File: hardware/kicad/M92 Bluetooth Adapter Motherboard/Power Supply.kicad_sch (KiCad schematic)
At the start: 32 parts, among them IC2 L7805CDT-TR, IC4 NJU7031D, IC4 TL7660IDR, J1 Conn_External_Power, J4 B2B-XH-A, J5 B2B-XH-A, J9 B6B-XH-A, K3 HE3621A1210, K4 HE3621A1210, Q2 PN2222ATA

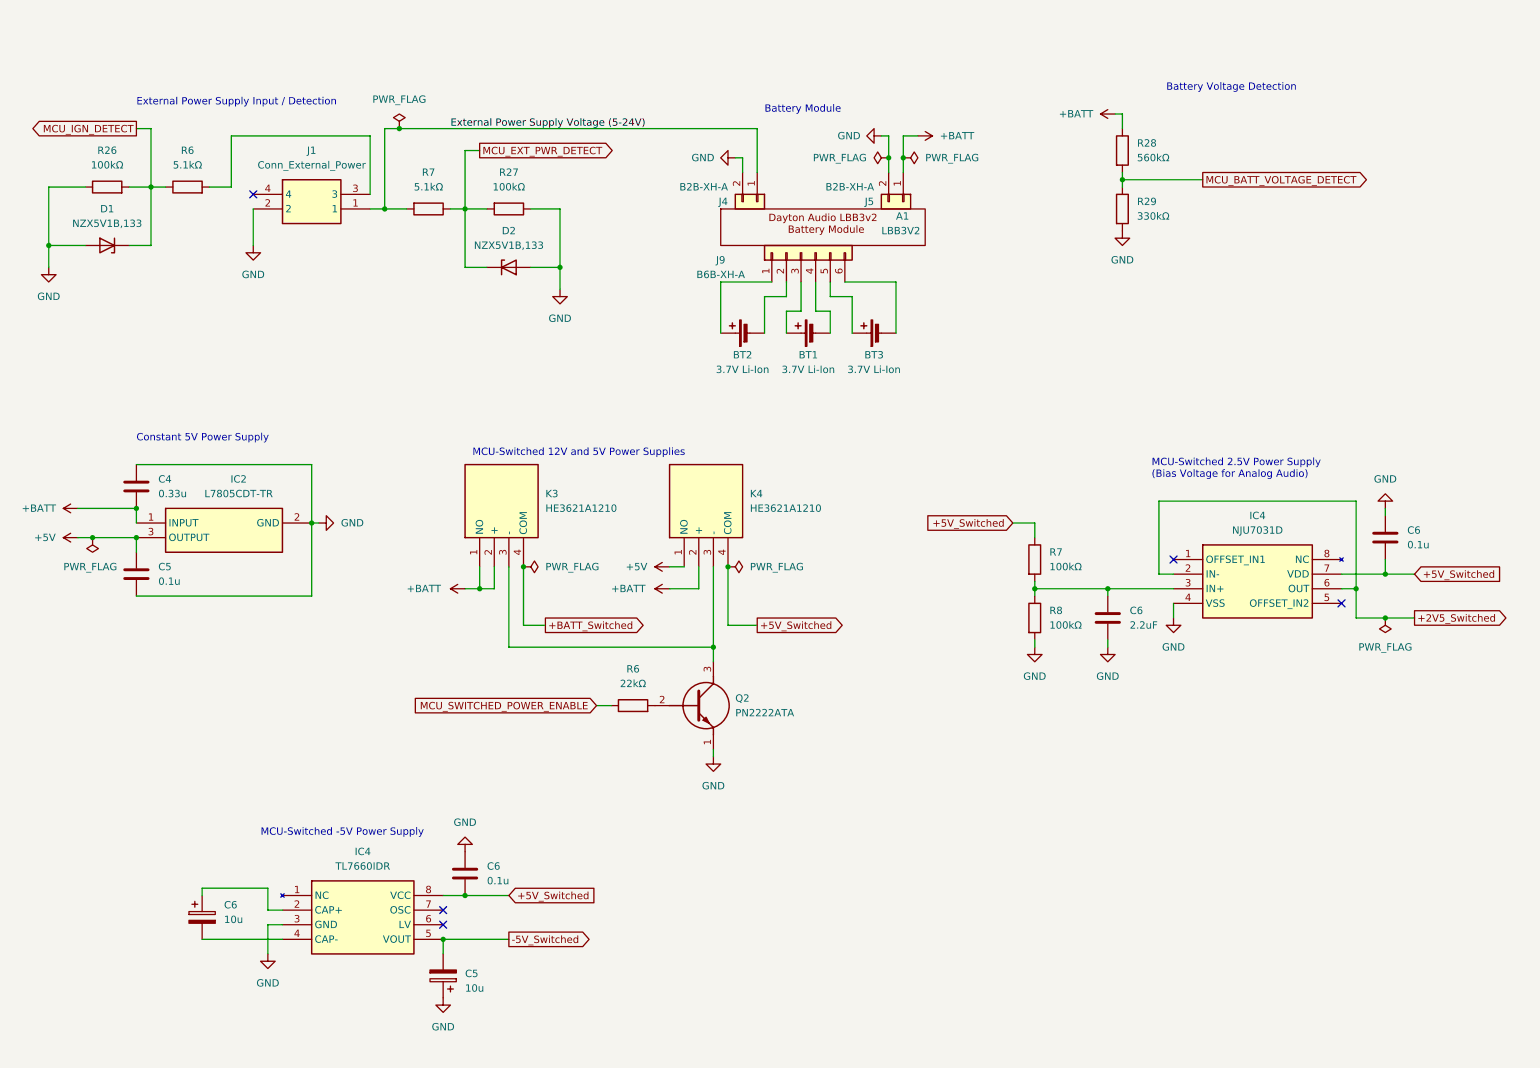
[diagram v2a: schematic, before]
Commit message: Update circuit/PCB to use different power supply/switching components
* Use more efficient 5V regulator.
* Use load switch ICs instead of reed switch relays for power switching.
* Swapped MCU pins for battery voltage detect and power switching for better PCB layout.
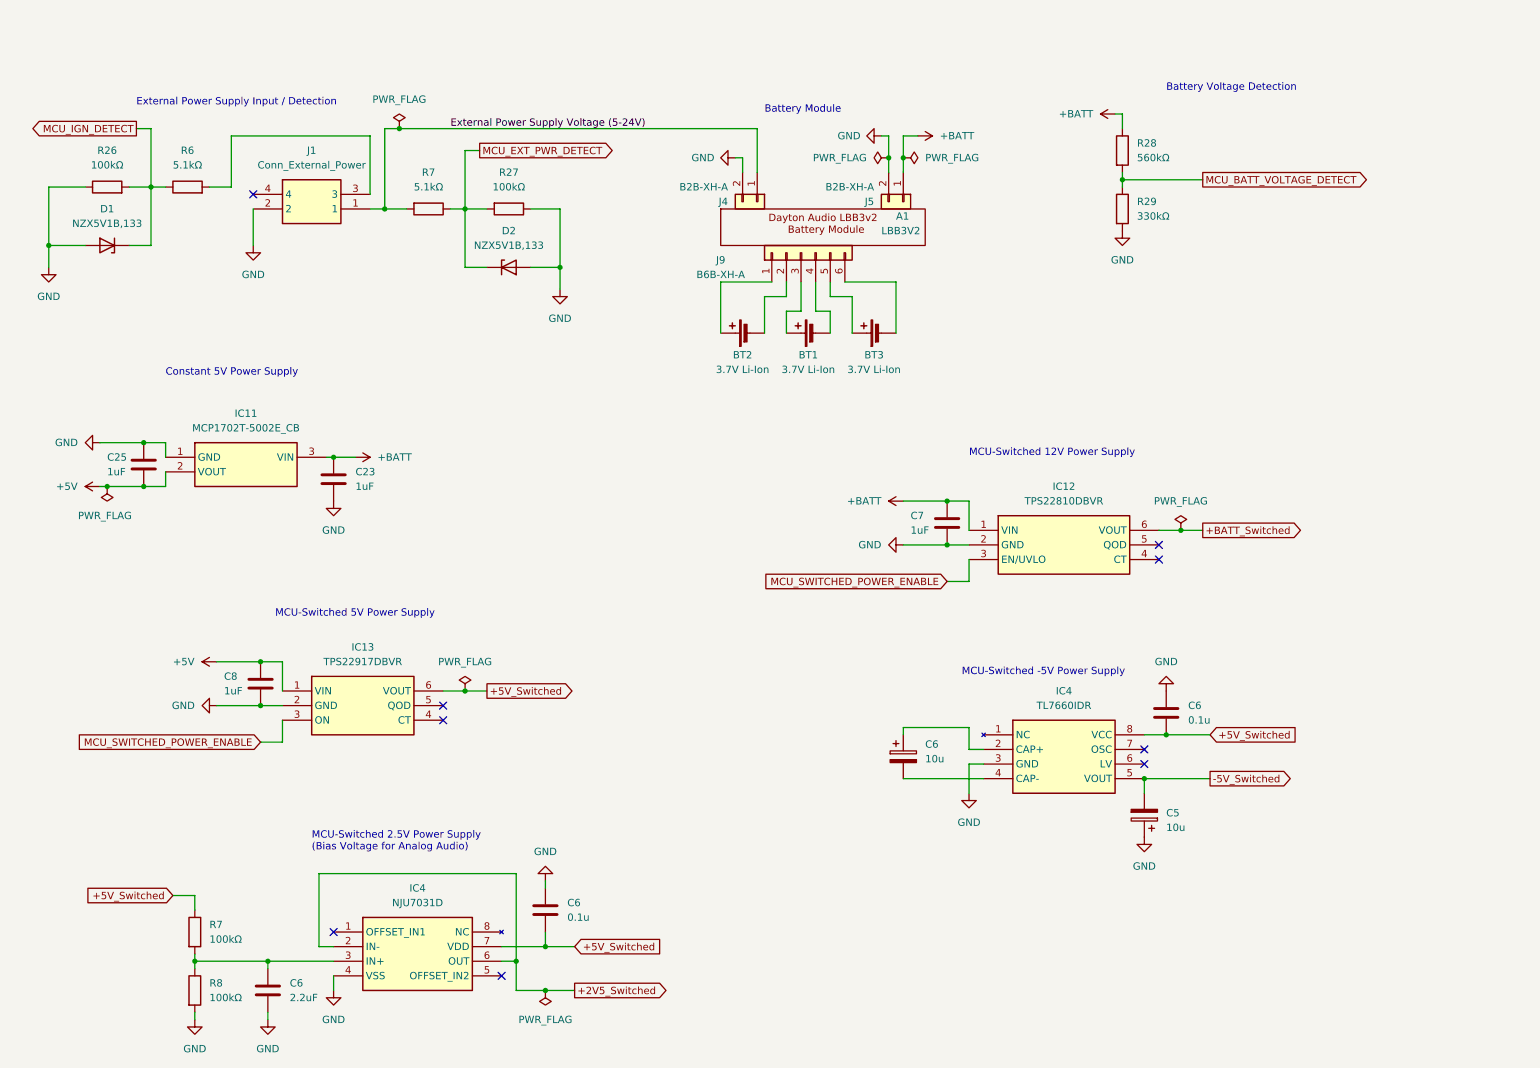
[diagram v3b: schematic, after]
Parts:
- removed C4: 0.33u, Capacitor_SMD:C_1206_3216Metric_Pad1.33x1.80mm_HandSolder, symbol Device:C
- removed C5: 0.1u, Capacitor_SMD:C_1206_3216Metric_Pad1.33x1.80mm_HandSolder, symbol Device:C
- removed IC2: L7805CDT-TR, L7805CDTTR, symbol SamacSys_Parts:L7805CDT-TR
- removed K3, K4: HE3621A1210, HE3621A1210, symbol SamacSys_Parts:HE3621A1210
- removed Q2: PN2222ATA, BC33740TA, symbol SamacSys_Parts:PN2222ATA
- removed R6: 22kΩ, Resistor_SMD:R_1206_3216Metric_Pad1.30x1.75mm_HandSolder, symbol Device:R
- added C23, C25, C7, C8: 1uF, Capacitor_SMD:C_1206_3216Metric_Pad1.33x1.80mm_HandSolder, symbol Device:C
- added IC11: MCP1702T-5002E_CB, SOT95P255X145-3N, symbol SamacSys_Parts:MCP1702T-5002E_CB
- added IC12: TPS22810DBVR, SOT95P280X145-6N, symbol SamacSys_Parts:TPS22810DBVR
- added IC13: TPS22917DBVR, SOT95P280X145-6N, symbol SamacSys_Parts:TPS22917DBVR
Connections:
- net +5V: now also C25.2, C8.1, IC11.2 (VOUT), IC13.1 (VIN)
- net +5V_Switched: now also IC13.6 (VOUT)
- net +BATT: now also C23.1, C7.1, IC11.3 (VIN), IC12.1 (VIN)
- net +BATT_Switched: now also IC12.6 (VOUT)
- net GND: now also C23.2, C25.1, C7.2, C8.2, IC11.1 (GND), IC12.2 (GND), IC13.2 (GND)
- net MCU_SWITCHED_POWER_ENABLE: now also IC12.3 (EN/UVLO), IC13.3 (ON)
- no-connect marks 5 -> 9
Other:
- note added: "MCU-Switched 12V Power Supply"
- note added: "MCU-Switched 5V Power Supply"
- note removed: "MCU-Switched 12V and 5V Power Supplies"
- moved on the sheet: C5, C6, IC4, R7, R8

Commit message: Motherboard circuit/PCB adjustments
* Add 100uf cap to stabilize the 5V power supply (reduce voltage dip during power-on of switched 5V supply).
* Add cap to 12V load switch to reduce inrush current when powering on handset.
* Part number updates to more readily available parts.
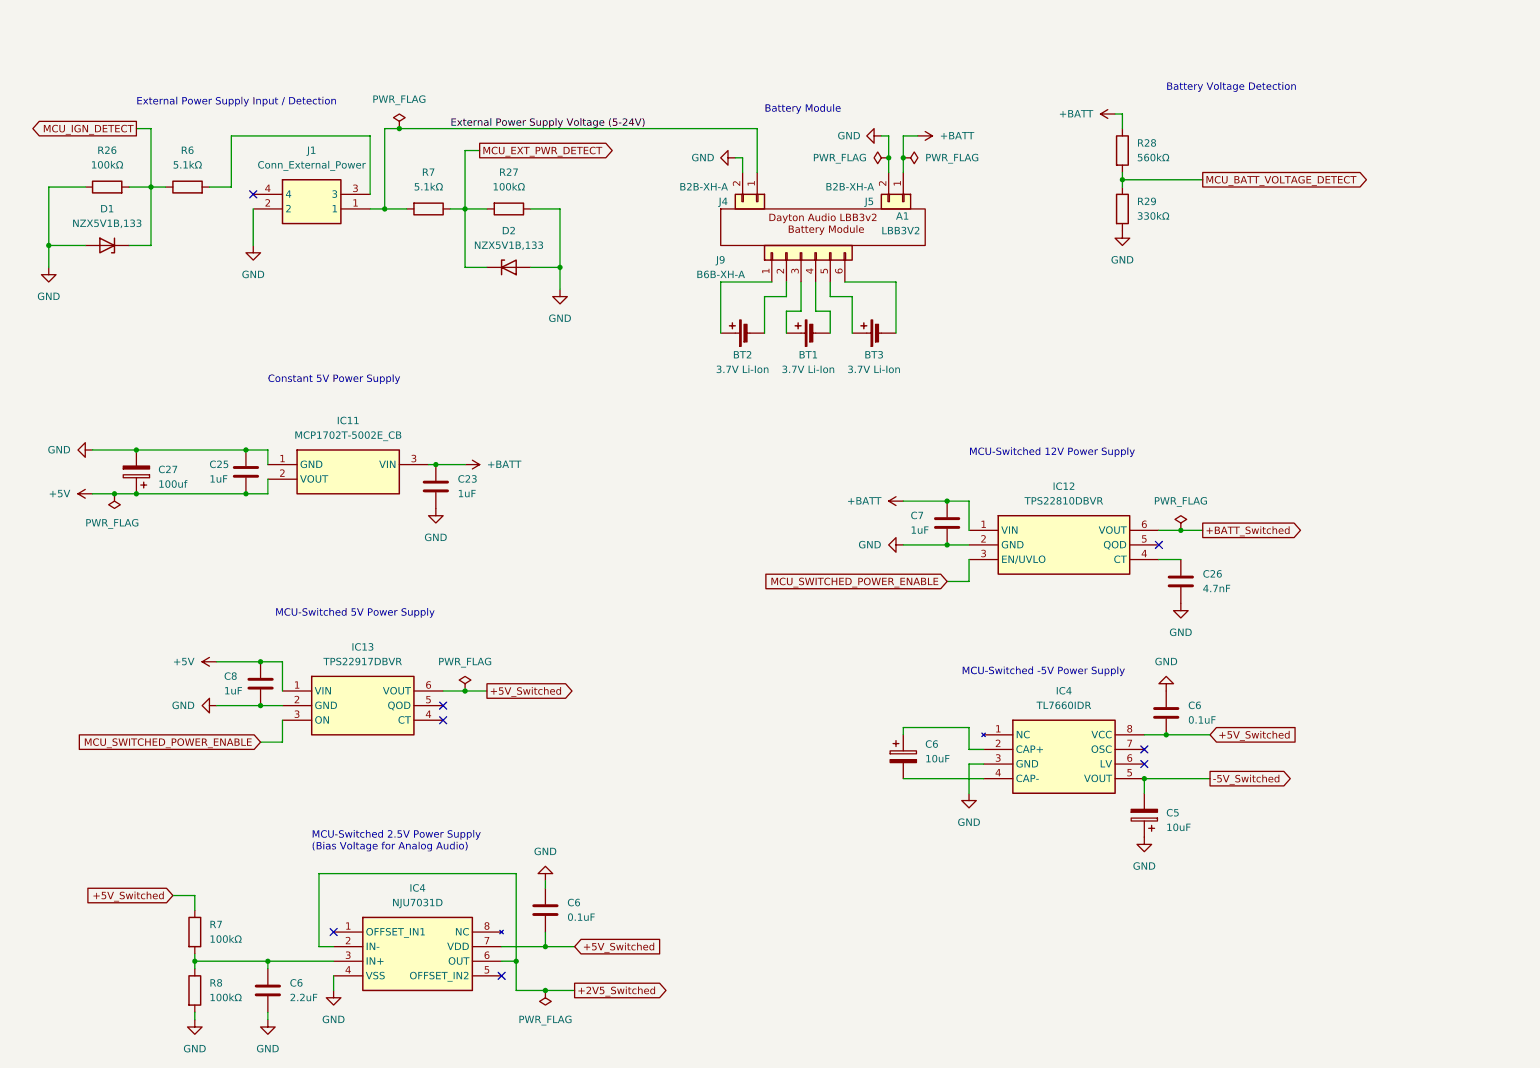
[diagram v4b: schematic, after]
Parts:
- added C26: 4.7nF, Capacitor_SMD:C_1206_3216Metric_Pad1.33x1.80mm_HandSolder, symbol Device:C
- added C27: 100uf, Capacitor_SMD:CP_Elec_5x5.4, symbol Device:C_Polarized
- C5, C6: value 10u -> 10uF; JLCPCB Part # C3001227 -> C473425
- C6: JLCPCB Part # C5137587 -> C454096
- C6: value 0.1u -> 0.1uF
- IC11: JLCPCB Part # (none) -> C180192
- IC12: JLCPCB Part # (none) -> C205990
- IC13: JLCPCB Part # (none) -> C2681320
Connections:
- net +5V: now also C27.1
- net GND: now also C26.2, C27.2
- net at IC12.4 (CT): now also C26.1
- no-connect marks 9 -> 8
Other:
- moved on the sheet: C23, C25, IC11

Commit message: Keep handset powered on during restarts
Inverted the switched power enable signal from the MCU with a transistor so that switched power is on by default unless the MCU explicitly disables it. This allows everything to remain powered on while the MCU reboots for a restart. If the MCU is rebooting to power off, then it immediately turns switched power off before entering the sleep state.

This is simpler and more robust than attempting to write code to fully reinitialize ALL MCU state/memory except for switched power enable output.
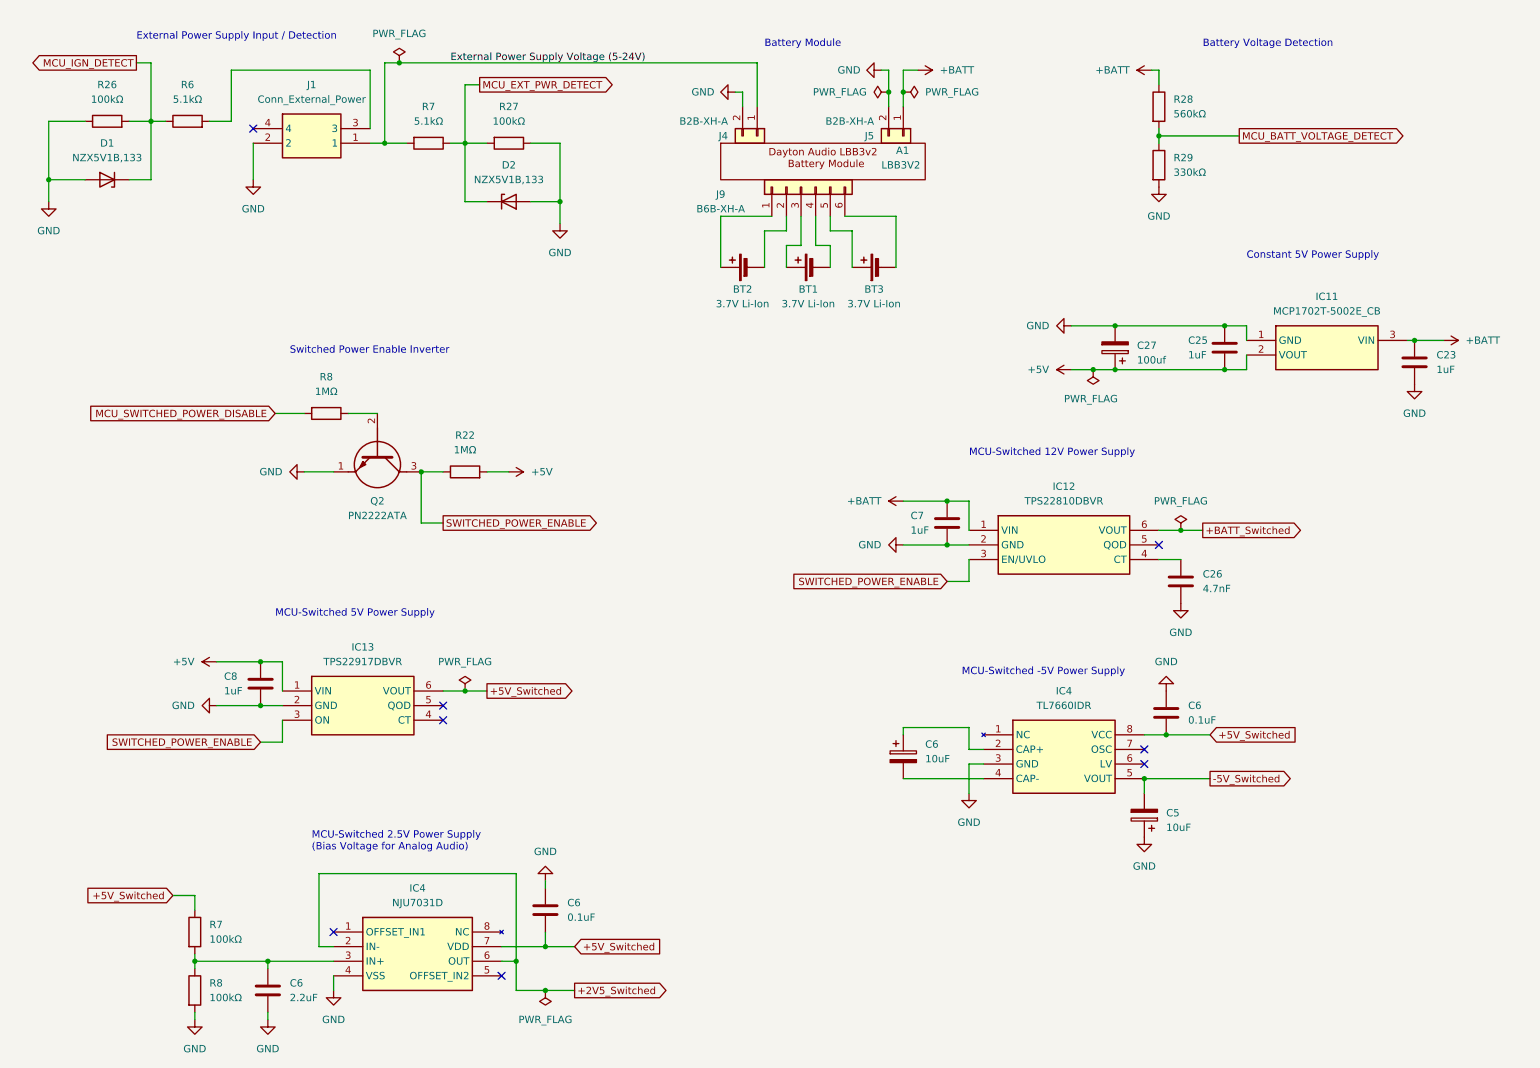
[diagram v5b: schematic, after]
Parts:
- added Q2: PN2222ATA, BC33740TA, symbol SamacSys_Parts:PN2222ATA
- added R22, R8: 1MΩ, Resistor_SMD:R_1206_3216Metric_Pad1.30x1.75mm_HandSolder, symbol Device:R
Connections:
- net +5V: now also R22.2
- net GND: now also Q2.1 (E)
- net MCU_SWITCHED_POWER_ENABLE renamed SWITCHED_POWER_ENABLE
- net SWITCHED_POWER_ENABLE: now also Q2.3 (C), R22.1
- new net: Q2.2 (B), R8.1
- new net MCU_SWITCHED_POWER_DISABLE: R8.2
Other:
- note added: "Switched Power Enable Inverter"
- moved on the sheet: A1, BT1, BT2, BT3, C23, C25, C27, D1, D2, IC11, J1, J4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

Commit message: Simplify load switch enable circuit, and add 100uF cap to 12V supply
Eliminated the load switch enable inverting transistor and simplified to a combination of a pull-up resistor on the enable pin with open-drain and initially high configuration of the MCU pin.

This still keeps the load switches enabled during a MCU reboot like the previous design, but with fewer components and less wasted power.

Also added a 100uF capacitor to the 12V supply to help reduce voltage dips.
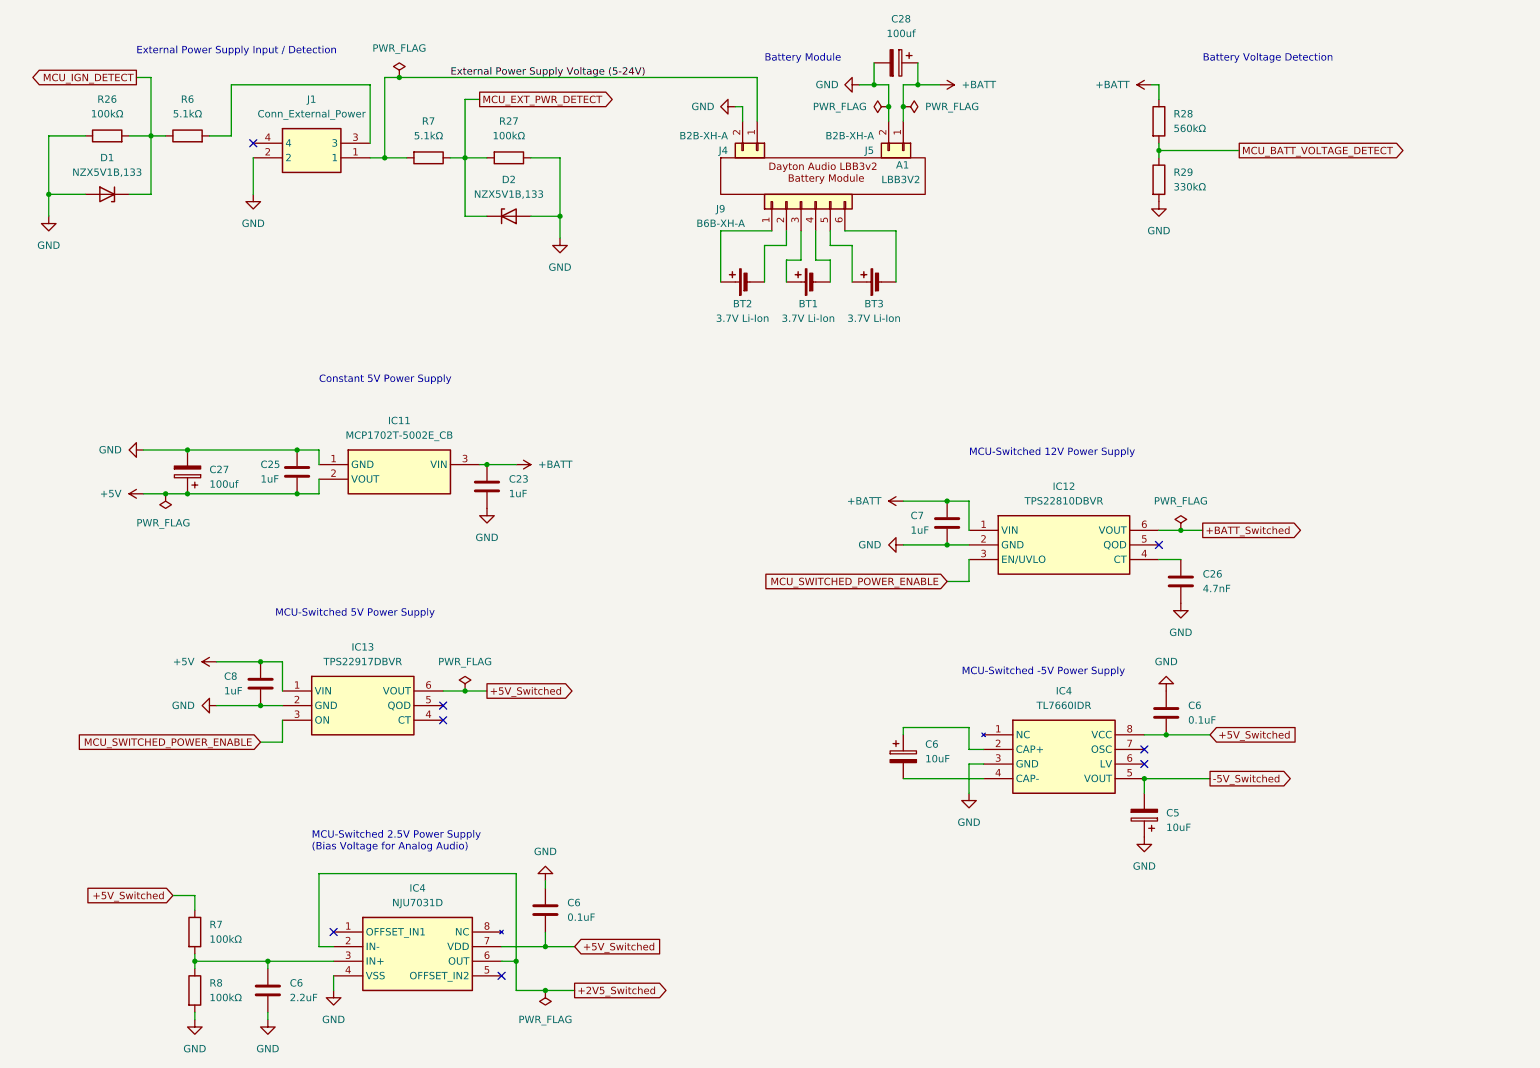
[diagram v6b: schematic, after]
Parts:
- removed Q2: PN2222ATA, BC33740TA, symbol SamacSys_Parts:PN2222ATA
- removed R22, R8: 1MΩ, Resistor_SMD:R_1206_3216Metric_Pad1.30x1.75mm_HandSolder, symbol Device:R
- added C28: 100uf, Capacitor_SMD:CP_Elec_5x5.4, symbol Device:C_Polarized
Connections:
- net +BATT: now also C28.1
- net GND: now also C28.2
- net SWITCHED_POWER_ENABLE renamed MCU_SWITCHED_POWER_ENABLE
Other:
- note removed: "Switched Power Enable Inverter"
- moved on the sheet: A1, BT1, BT2, BT3, C23, C25, C27, D1, D2, IC11, J1, J4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
